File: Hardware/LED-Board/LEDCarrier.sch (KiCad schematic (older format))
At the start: 7 parts, among them IC1 ATTINY48-M, P1 CONN_01X04, P2 CONN_01X04, P3 CONN_02X04

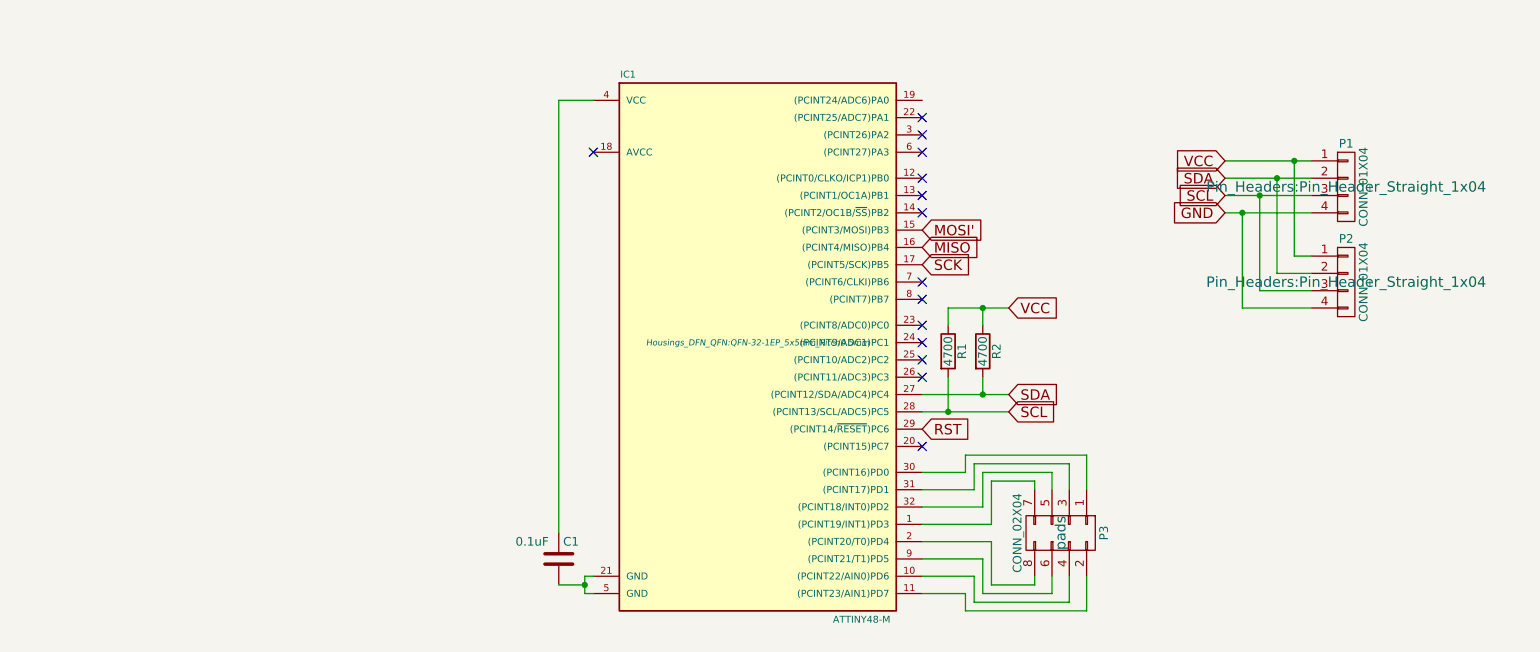
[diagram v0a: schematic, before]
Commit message: Finished Schematic, Started Layout
Finished schematic and layout of color sensor as well
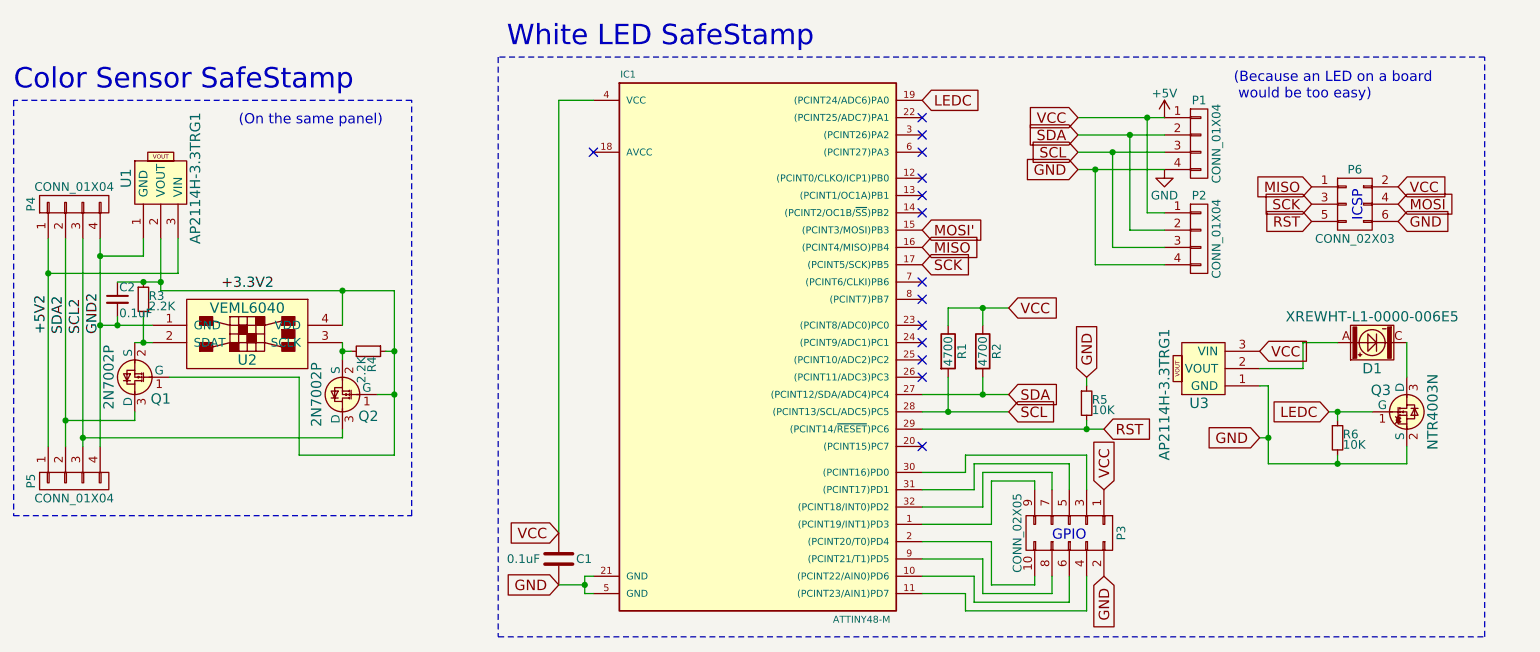
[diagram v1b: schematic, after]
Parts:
- removed P3: CONN_02X04, pads, symbol CONN_02X04
- added C2: 0.1uF, Capacitors_SMD:C_0603, symbol C_Small
- added D1: XREWHT-L1-0000-006E5, RST-Footprints:XR-E-2-SMD, symbol XREWHT-L1-0000-006E5
- added P3: CONN_02X05, RST-Footprints:PAD-2x5, symbol CONN_02X05
- added P4, P5: CONN_01X04, Pin_Headers:Pin_Header_Straight_1x04, symbol CONN_01X04
- added P6: CONN_02X03, Pin_Headers:Pin_Header_Straight_2x03, symbol CONN_02X03
- added Q1, Q2: 2N7002P, Housings_SOT-23_SOT-143_TSOT-6:SOT-23, symbol 2N7002P
- added Q3: NTR4003N, Housings_SOT-23_SOT-143_TSOT-6:SOT-23, symbol NTR4003N
- added R3, R4: 2.2K, Resistors_SMD:R_0603, symbol R_Small
- added R5, R6: 10K, Resistors_SMD:R_0603, symbol R_Small
- added U1, U3: AP2114H-3.3TRG1, RST-Footprints:SOT223, symbol AP2114H-3.3TRG1
- added U2: VEML6040, RST-Footprints:4-TFLGA, symbol VEML6040
- C1: footprint (none) -> Capacitors_SMD:C_0603; Digikey PN (none) -> 311-1335-1-ND
- R1, R2: footprint (none) -> Resistors_SMD:R_0603; Digikey PN (none) -> RHM4.7KDCT-ND
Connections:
- net VCC is gone; now on net +5V: P1.1 (P1), P2.1 (P1), R1.1, R2.1
- net GND: now also C1.2, IC1.21 (GND), IC1.5 (GND), P3.2 (P2), P6.6 (P6), Q3.2 (S), R5.1, R6.2, U3.1 (GND)
- net MISO: now also P6.1 (P1)
- net RST: now also P6.5 (P5), R5.2
- net SCK: now also P6.3 (P3)
- net at IC1.1 ((PCINT19/INT1)PD3): now also P3.9 (P9)
- net at IC1.10 ((PCINT22/AIN0)PD6): now also P3.6 (P6)
- net at IC1.11 ((PCINT23/AIN1)PD7): now also P3.4 (P4)
- net LEDC: now reaches IC1.19 ((PCINT24/ADC6)PA0)
- net LEDC: now also Q3.1 (G), R6.1
- net at IC1.2 ((PCINT20/T0)PD4): now also P3.10 (P10)
- net at IC1.30 ((PCINT16)PD0): now also P3.3 (P3)
- net at IC1.31 ((PCINT17)PD1): now also P3.5 (P5)
- net at IC1.32 ((PCINT18/INT0)PD2): now also P3.7 (P7)
- net +5V: now reaches C1.1, IC1.4 (VCC)
- net +5V: now also P3.1 (P1), P6.2 (P2), U3.3 (VIN)
- net at IC1.9 ((PCINT21/T1)PD5): now also P3.8 (P8)
- new net: Q1.2 (S), R3.2, U2.2 (SDAT)
- new net: Q2.2 (S), R4.2, U2.3 (SCLK)
- new net: D1.A, U3.2 (VOUT)
- new net: D1.C, Q3.3 (D)
- new net +3.3V2: C2.1, Q1.1 (G), Q2.1 (G), R3.1, R4.1, U1.2 (VOUT), U2.4 (VDD)
- new net +5V2: P4.1 (P1), P5.1 (P1), U1.3 (VIN)
- new net GND2: C2.2, P4.4 (P4), P5.4 (P4), U1.1 (GND), U2.1 (GND)
- new net MOSI: P6.4 (P4)
- new net SCL2: P4.3 (P3), P5.3 (P3), Q2.3 (D)
- new net SDA2: P4.2 (P2), P5.2 (P2), Q1.3 (D)
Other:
- note added: "(Because an LED on a board\n would be too easy)"
- note added: "(On the same panel)\n"
- note added: "Color Sensor SafeStamp\n"
- note added: "GPIO\n"
- note added: "ICSP"
- note added: "White LED SafeStamp"
- moved on the sheet: P1, P2
